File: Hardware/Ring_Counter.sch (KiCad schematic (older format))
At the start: 83 parts, among them Q10 BC848, Q11 BC848, Q12 BC848, Q13 BC848, Q14 BC848, Q15 BC848, Q16 BC848, Q17 BC848, Q18 BC848, Q19 BC848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

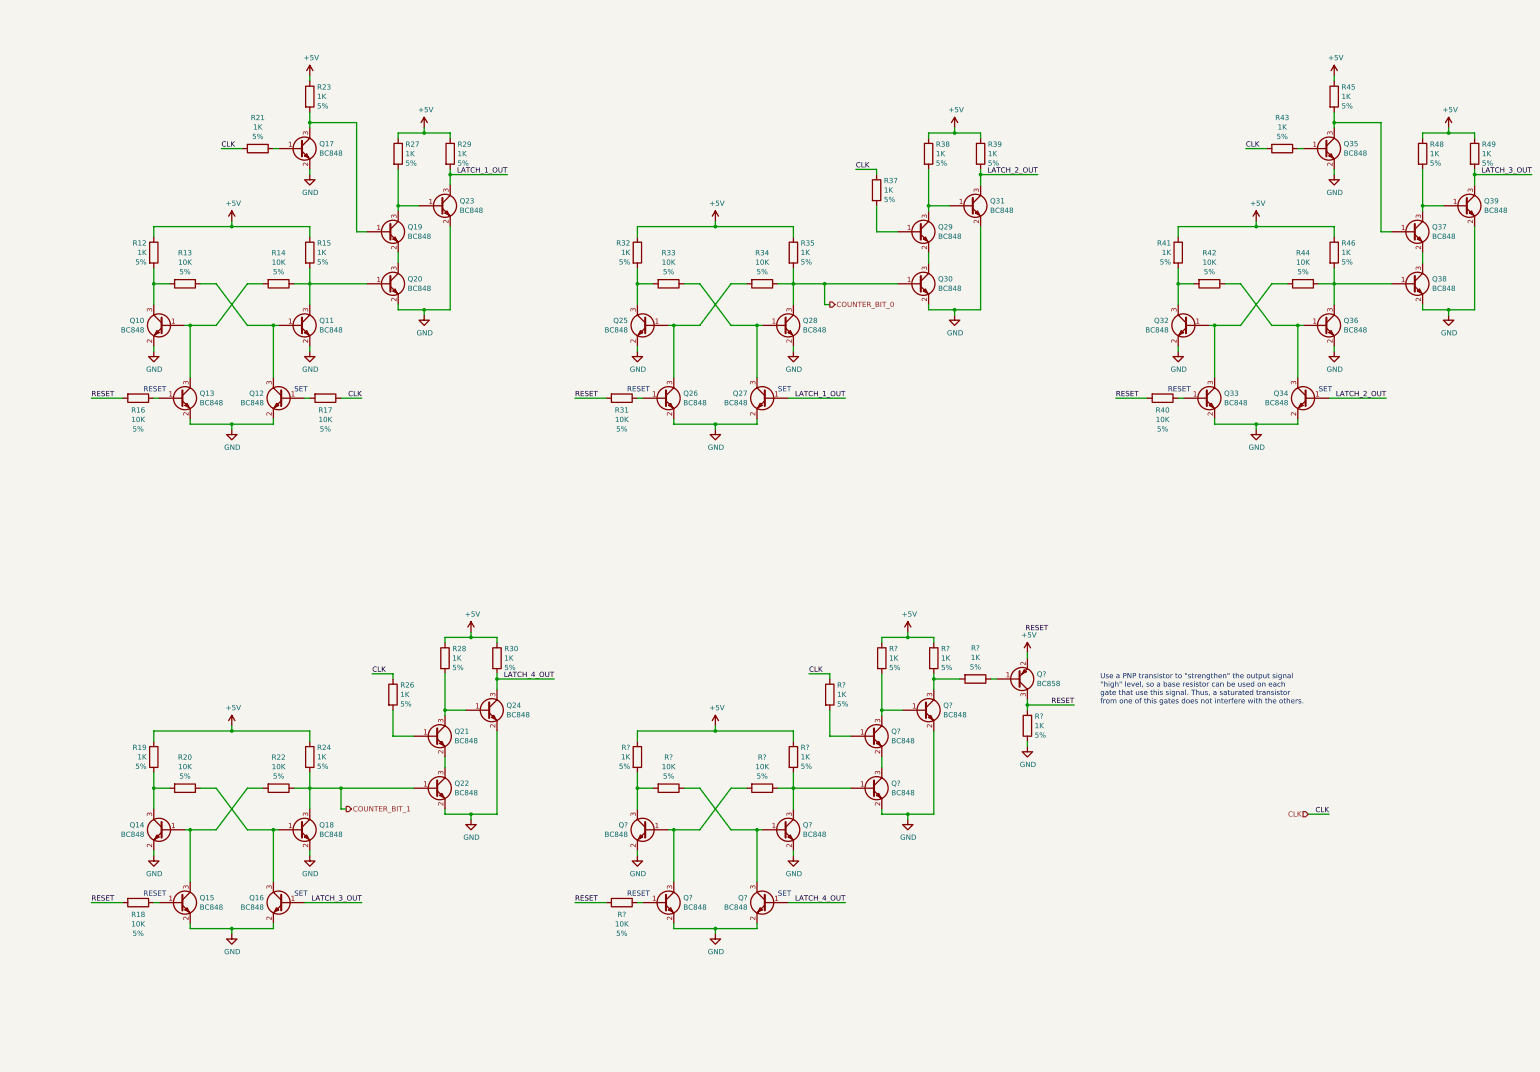
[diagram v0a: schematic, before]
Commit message: Improved ring counter RS latches output with better signal quality and less transistors count.
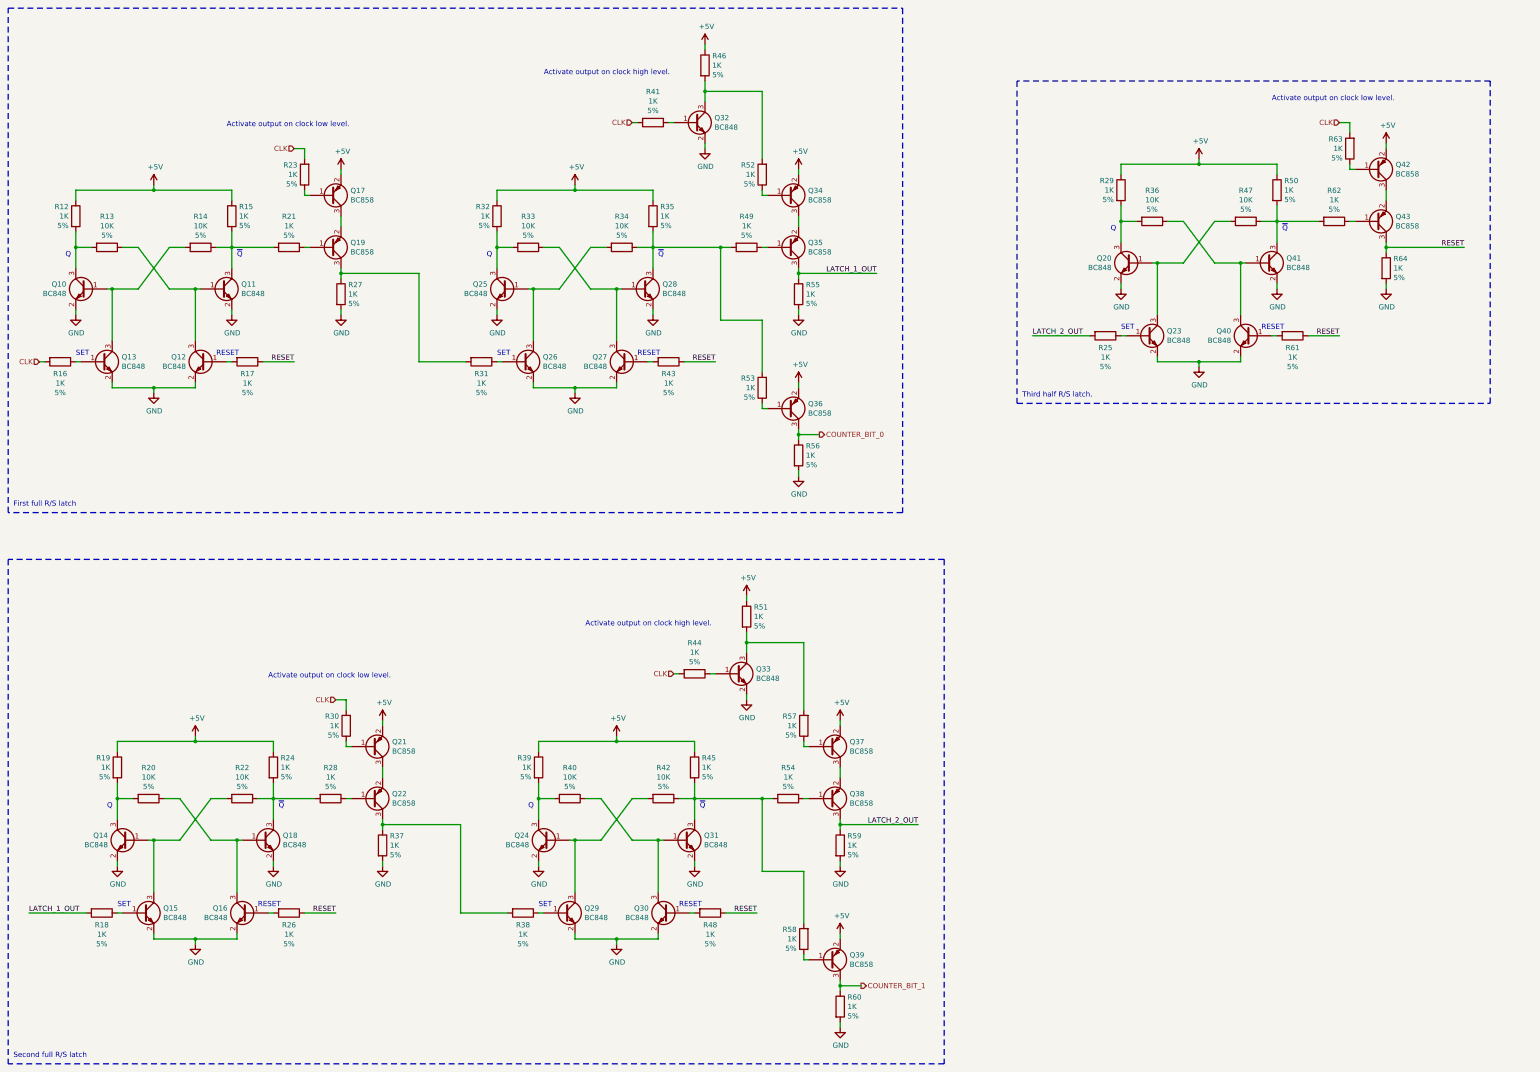
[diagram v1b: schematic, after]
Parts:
- removed Q17, Q19, Q20, Q21, Q22, Q23, Q34, Q35, Q36, Q37, Q38, Q39, Q? (x3): BC848, Package_TO_SOT_SMD:SOT-23, symbol Transistor_BJT:BC848
- removed Q?: BC858, Package_TO_SOT_SMD:SOT-23, symbol Transistor_BJT:BC858
- removed R29, R? (x5): 1K, Resistor_SMD:R_0603_1608Metric_Pad0.98x0.95mm_HandSolder, symbol Device:R
- added Q17, Q19, Q21, Q22, Q34, Q35, Q36, Q37, Q38, Q39, Q42, Q43: BC858, Package_TO_SOT_SMD:SOT-23, symbol Transistor_BJT:BC858
- added R51, R52, R53, R54, R55, R56, R57, R58, R59, R60, R61, R62, R63, R64: 1K, Resistor_SMD:R_0603_1608Metric_Pad0.98x0.95mm_HandSolder, symbol Device:R
- R16, R17, R18, R31: value 10K -> 1K
- R21, R23, R26, R28, R30, R38, R43, R48, R49: Spice_Model 1k -> 10k
- R25: renamed from R?; value 10K -> 1K
- R44: value 10K -> 1K; Spice_Model 10k -> 1k
- gave numbers to parts that had none: 8
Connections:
- net +5V: now also Q17.2 (E), Q21.2 (E), Q34.2 (E), Q36.2 (E), Q37.2 (E), Q39.2 (E), Q42.2 (E), R51.1; no longer R23.1, R27.1, R28.1, R30.1, R38.1, R41.1, R48.1, R49.1
- net CLK: now also R16.2, R23.2, R30.2, R41.2, R44.2, R63.2; no longer R17.1, R21.2, R26.1, R37.1, R43.2
- net COUNTER_BIT_0: now also Q36.3 (C), R56.1; no longer Q28.3 (C), Q30.1 (B), R34.1, R35.2
- net COUNTER_BIT_1: now also Q39.3 (C), R60.1; no longer Q18.3 (C), R22.1, R24.2
- net GND: now also Q29.2 (E), R27.2, R37.2, R55.2, R56.2, R59.2, R60.2, R64.2
- net LATCH_1_OUT: now also R18.2, Q35.3 (C), R55.1; no longer Q27.1 (B)
- net LATCH_2_OUT: now also R25.2, Q38.3 (C), R59.1; no longer Q31.3 (C), R39.2
- net RESET: now also R17.1, R26.1, R43.1, R48.1, Q43.3 (C), R61.1, R64.1; no longer R16.2, R18.2, R25.2, R31.2, R40.2
- net at Q11.3 (C), R14.1, R15.2: now also R21.2
- net at R21.1: now also Q19.1 (B)
- net at Q29.1 (B): now also R38.1; no longer R37.2
- net at Q30.3 (C): now also Q31.1 (B), R40.1; no longer Q29.2 (E)
- net at R45.2: now also Q31.3 (C), R42.1, R54.2, R58.2
- net at R48.2: now also Q30.1 (B)
- net at R46.2: now also Q32.3 (C), R52.2; no longer R44.1
- net at Q33.1 (B): now also R44.1; no longer R40.1
- net at R26.2: now also Q16.1 (B)
- net at R28.2: now also Q18.3 (C), R22.1, R24.2; no longer Q24.1 (B)
- net at Q41.3 (C), R47.1, R50.2: now also R62.2
- net LATCH_3_OUT: no longer names the net of R49.2
- net LATCH_3_OUT: now also Q28.3 (C), R34.1, R35.2, R53.2; no longer Q16.1 (B)
- removed net LATCH_4_OUT: Q24.3 (C), Q40.1 (B), R30.2
- new net: Q19.3 (C), R27.1, R31.2
- new net: Q27.1 (B), R43.2
- new net: Q40.1 (B), R61.2
- new net: Q35.1 (B), R49.1
- new net: Q34.3 (C), Q35.2 (E)
- new net: Q34.1 (B), R52.1
- new net: Q32.1 (B), R41.1
- new net: Q36.1 (B), R53.1
- new net: Q24.1 (B), Q29.3 (C), R42.2
- new net: Q24.3 (C), R39.2, R40.2
- new net: Q22.3 (C), R37.1, R38.2
- new net: Q22.1 (B), R28.1
- new net: Q21.3 (C), Q22.2 (E)
- new net: Q21.1 (B), R30.1
- new net: Q33.3 (C), R51.2, R57.2
- new net: Q39.1 (B), R58.1
- new net: Q37.1 (B), R57.1
- new net: Q37.3 (C), Q38.2 (E)
- new net: Q38.1 (B), R54.1
- new net: Q17.3 (C), Q19.2 (E)
- new net: Q17.1 (B), R23.1
- new net: Q43.1 (B), R62.1
- new net: Q42.3 (C), Q43.2 (E)
- new net: Q42.1 (B), R63.1
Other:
- note added: "Activate output on clock high level."
- note added: "Activate output on clock low level."
- note added: "First full R/S latch"
- note added: "Q"
- note added: "Second full R/S latch"
- note added: "Third half R/S latch."
- note added: "~Q~"
- note removed: "Use a PNP transistor to "strengthen" the output signal\n"high" level, so a base resistor can be used on each\ngate that use this signal. Thus, a saturated transistor\nfrom one of this gates does not interfere with the others."
- moved on the sheet: Q10, Q11, Q12, Q13, Q20, Q23, Q25, Q26, Q27, Q28, Q40, Q41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

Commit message: Added second led logic and power transistor, also added BC858 SPICE model.
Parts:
- Q17, Q19, Q21, Q22, Q34, Q35, Q36, Q37, Q38, Q39, Q42, Q43: Spice_Lib_File (none) -> Spice_Simulation/BC858.lib; Spice_Model (none) -> BC858; Spice_Netlist_Enabled (none) -> Y; Spice_Node_Sequence (none) -> 3 1 2; Spice_Primitive (none) -> Q
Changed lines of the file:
@@
 F 2 "Package_TO_SOT_SMD:SOT-23" H 3900 2975 50  0001 L CIN
 F 3 "https://www.onsemi.com/pub/Collateral/BC860-D.pdf" H 3700 3050 50  0001 L CNN
+F 4 "Spice_Simulation/BC858.lib" H 3700 3050 50  0001 C CNN "Spice_Lib_File"
+F 5 "BC858" H 3700 3050 50  0001 C CNN "Spice_Model"
+F 6 "Y" H 3700 3050 50  0001 C CNN "Spice_Netlist_Enabled"
+F 7 "Q" H 3700 3050 50  0001 C CNN "Spice_Primitive"
+F 8 "3 1 2" H 3700 3050 50  0001 C CNN "Spice_Node_Sequence"
 	1    3700 3050
 	1    0    0    1
@@
 F 2 "Package_TO_SOT_SMD:SOT-23" H 3900 2475 50  0001 L CIN
 F 3 "https://www.onsemi.com/pub/Collateral/BC860-D.pdf" H 3700 2550 50  0001 L CNN
+F 4 "Q" H 3700 2550 50  0001 C CNN "Spice_Primitive"
+F 5 "BC858" H 3700 2550 50  0001 C CNN "Spice_Model"
+F 6 "Y" H 3700 2550 50  0001 C CNN "Spice_Netlist_Enabled"
+F 7 "Spice_Simulation/BC858.lib" H 3700 2550 50  0001 C CNN "Spice_Lib_File"
+F 8 "3 1 2" H 3700 2550 50  0001 C CNN "Spice_Node_Sequence"
 	1    3700 2550
 	1    0    0    1
@@
 F 2 "Package_TO_SOT_SMD:SOT-23" H 8300 4525 50  0001 L CIN
 F 3 "https://www.onsemi.com/pub/Collateral/BC860-D.pdf" H 8100 4600 50  0001 L CNN
+F 4 "Spice_Simulation/BC858.lib" H 8100 4600 50  0001 C CNN "Spice_Lib_File"
+F 5 "BC858" H 8100 4600 50  0001 C CNN "Spice_Model"
+F 6 "Y" H 8100 4600 50  0001 C CNN "Spice_Netlist_Enabled"
+F 7 "Q" H 8100 4600 50  0001 C CNN "Spice_Primitive"
+F 8 "3 1 2" H 8100 4600 50  0001 C CNN "Spice_Node_Sequence"
 	1    8100 4600
 	1    0    0    1
@@
 F 2 "Package_TO_SOT_SMD:SOT-23" H 8300 2475 50  0001 L CIN
 F 3 "https://www.onsemi.com/pub/Collateral/BC860-D.pdf" H 8100 2550 50  0001 L CNN
+F 4 "Spice_Simulation/BC858.lib" H 8100 2550 50  0001 C CNN "Spice_Lib_File"
+F 5 "BC858" H 8100 2550 50  0001 C CNN "Spice_Model"
+F 6 "Y" H 8100 2550 50  0001 C CNN "Spice_Netlist_Enabled"
+F 7 "Q" H 8100 2550 50  0001 C CNN "Spice_Primitive"
+F 8 "3 1 2" H 8100 2550 50  0001 C CNN "Spice_Node_Sequence"
 	1    8100 2550
 	1    0    0    1
@@
 F 2 "Package_TO_SOT_SMD:SOT-23" H 8300 2975 50  0001 L CIN
 F 3 "https://www.onsemi.com/pub/Collateral/BC860-D.pdf" H 8100 3050 50  0001 L CNN
+F 4 "Spice_Simulation/BC858.lib" H 8100 3050 50  0001 C CNN "Spice_Lib_File"
+F 5 "BC858" H 8100 3050 50  0001 C CNN "Spice_Model"
+F 6 "Y" H 8100 3050 50  0001 C CNN "Spice_Netlist_Enabled"
+F 7 "Q" H 8100 3050 50  0001 C CNN "Spice_Primitive"
+F 8 "3 1 2" H 8100 3050 50  0001 C CNN "Spice_Node_Sequence"
 	1    8100 3050
 	1    0    0    1
@@
 F 2 "Package_TO_SOT_SMD:SOT-23" H 4300 8275 50  0001 L CIN
 F 3 "https://www.onsemi.com/pub/Collateral/BC860-D.pdf" H 4100 8350 50  0001 L CNN
+F 4 "Spice_Simulation/BC858.lib" H 4100 8350 50  0001 C CNN "Spice_Lib_File"
+F 5 "BC858" H 4100 8350 50  0001 C CNN "Spice_Model"
+F 6 "Y" H 4100 8350 50  0001 C CNN "Spice_Netlist_Enabled"
+F 7 "Q" H 4100 8350 50  0001 C CNN "Spice_Primitive"
+F 8 "3 1 2" H 4100 8350 50  0001 C CNN "Spice_Node_Sequence"
 	1    4100 8350
 	1    0    0    1
@@
 F 2 "Package_TO_SOT_SMD:SOT-23" H 4300 7775 50  0001 L CIN
 F 3 "https://www.onsemi.com/pub/Collateral/BC860-D.pdf" H 4100 7850 50  0001 L CNN
+F 4 "Spice_Simulation/BC858.lib" H 4100 7850 50  0001 C CNN "Spice_Lib_File"
+F 5 "BC858" H 4100 7850 50  0001 C CNN "Spice_Model"
+F 6 "Y" H 4100 7850 50  0001 C CNN "Spice_Netlist_Enabled"
+F 7 "Q" H 4100 7850 50  0001 C CNN "Spice_Primitive"
+F 8 "3 1 2" H 4100 7850 50  0001 C CNN "Spice_Node_Sequence"
 	1    4100 7850
 	1    0    0    1
@@
 F 2 "Package_TO_SOT_SMD:SOT-23" H 8700 9825 50  0001 L CIN
 F 3 "https://www.onsemi.com/pub/Collateral/BC860-D.pdf" H 8500 9900 50  0001 L CNN
+F 4 "Spice_Simulation/BC858.lib" H 8500 9900 50  0001 C CNN "Spice_Lib_File"
+F 5 "BC858" H 8500 9900 50  0001 C CNN "Spice_Model"
+F 6 "Y" H 8500 9900 50  0001 C CNN "Spice_Netlist_Enabled"
+F 7 "Q" H 8500 9900 50  0001 C CNN "Spice_Primitive"
+F 8 "3 1 2" H 8500 9900 50  0001 C CNN "Spice_Node_Sequence"
 	1    8500 9900
 	1    0    0    1
@@
 F 2 "Package_TO_SOT_SMD:SOT-23" H 8700 7775 50  0001 L CIN
 F 3 "https://www.onsemi.com/pub/Collateral/BC860-D.pdf" H 8500 7850 50  0001 L CNN
+F 4 "Spice_Simulation/BC858.lib" H 8500 7850 50  0001 C CNN "Spice_Lib_File"
+F 5 "BC858" H 8500 7850 50  0001 C CNN "Spice_Model"
+F 6 "Y" H 8500 7850 50  0001 C CNN "Spice_Netlist_Enabled"
+F 7 "Q" H 8500 7850 50  0001 C CNN "Spice_Primitive"
+F 8 "3 1 2" H 8500 7850 50  0001 C CNN "Spice_Node_Sequence"
 	1    8500 7850
 	1    0    0    1
@@
 F 2 "Package_TO_SOT_SMD:SOT-23" H 8700 8275 50  0001 L CIN
 F 3 "https://www.onsemi.com/pub/Collateral/BC860-D.pdf" H 8500 8350 50  0001 L CNN
+F 4 "Spice_Simulation/BC858.lib" H 8500 8350 50  0001 C CNN "Spice_Lib_File"
+F 5 "BC858" H 8500 8350 50  0001 C CNN "Spice_Model"
+F 6 "Y" H 8500 8350 50  0001 C CNN "Spice_Netlist_Enabled"
+F 7 "Q" H 8500 8350 50  0001 C CNN "Spice_Primitive"
+F 8 "3 1 2" H 8500 8350 50  0001 C CNN "Spice_Node_Sequence"
 	1    8500 8350
 	1    0    0    1
@@
 F 2 "Package_TO_SOT_SMD:SOT-23" H 13950 2725 50  0001 L CIN
 F 3 "https://www.onsemi.com/pub/Collateral/BC860-D.pdf" H 13750 2800 50  0001 L CNN
+F 4 "Spice_Simulation/BC858.lib" H 13750 2800 50  0001 C CNN "Spice_Lib_File"
+F 5 "BC858" H 13750 2800 50  0001 C CNN "Spice_Model"
+F 6 "Y" H 13750 2800 50  0001 C CNN "Spice_Netlist_Enabled"
+F 7 "Q" H 13750 2800 50  0001 C CNN "Spice_Primitive"
+F 8 "3 1 2" H 13750 2800 50  0001 C CNN "Spice_Node_Sequence"
 	1    13750 2800
 	1    0    0    1
@@
 F 2 "Package_TO_SOT_SMD:SOT-23" H 13950 2225 50  0001 L CIN
 F 3 "https://www.onsemi.com/pub/Collateral/BC860-D.pdf" H 13750 2300 50  0001 L CNN
+F 4 "Spice_Simulation/BC858.lib" H 13750 2300 50  0001 C CNN "Spice_Lib_File"
+F 5 "BC858" H 13750 2300 50  0001 C CNN "Spice_Model"
+F 6 "Y" H 13750 2300 50  0001 C CNN "Spice_Netlist_Enabled"
+F 7 "Q" H 13750 2300 50  0001 C CNN "Spice_Primitive"
+F 8 "3 1 2" H 13750 2300 50  0001 C CNN "Spice_Node_Sequence"
 	1    13750 2300
 	1    0    0    1

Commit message: Added RS latches power-on reset.
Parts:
- added C1: 4.7u, Capacitor_SMD:C_0805_2012Metric_Pad1.18x1.45mm_HandSolder, symbol Device:C
- added Q46: BC858, Package_TO_SOT_SMD:SOT-23, symbol Transistor_BJT:BC858
- added R70: 220K, Resistor_SMD:R_0603_1608Metric_Pad0.98x0.95mm_HandSolder, symbol Device:R
- added R71: 1K, Resistor_SMD:R_0603_1608Metric_Pad0.98x0.95mm_HandSolder, symbol Device:R
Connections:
- net +5V: now also Q46.2 (E), R70.2
- net GND: now also C1.2
- net RESET: now also Q46.3 (C)
- new net: C1.1, R70.1, R71.2
- new net: Q46.1 (B), R71.1
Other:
- note added: "First full RS latch."
- note added: "Power-on reset\nGenerate a 100ms high level pulse to reset latches."
- note added: "Second full RS latch."
- note added: "Third half RS latch."
- note removed: "First full R/S latch"
- note removed: "Second full R/S latch"
- note removed: "Third half R/S latch."
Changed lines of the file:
@@
 	600  5600 600  750
 Text Notes 650  5550 0    50   ~ 0
-First full R/S latch
+First full RS latch.
 Wire Notes Line
 	9600 6050 9600 10900
@@
 	600  6050 600  10900
 Text Notes 650  10850 0    50   ~ 0
-Second full R/S latch
+Second full RS latch.
 Text Label 9350 8600 2    50   ~ 0
 LATCH_2_OUT
@@
 	10300 4550 14850 4550
 Text Notes 10350 4500 0    50   ~ 0
-Third half R/S latch.
+Third half RS latch.
+$Comp
+L Device:R R?
+U 1 1 6211682E
+P 12300 7400
+AR Path="/6211682E" Ref="R?"  Part="1"
+AR Path="/61D90E9A/6211682E" Ref="R70"  Part="1"
+F 0 "R70" V 12003 7400 50  0000 C CNN
+F 1 "220K" V 12094 7400 50  0000 C CNN
+F 2 "Resistor_SMD:R_0603_1608Metric_Pad0.98x0.95mm_HandSolder" V 12230 7400 50  0001 C CNN
+F 3 "~" H 12300 7400 50  0001 C CNN
+F 4 "5%" V 12185 7400 50  0000 C CNN "Value2"
+F 5 "R" H 12300 7400 50  0001 C CNN "Spice_Primitive"
+F 6 "1k" H 12300 7400 50  0001 C CNN "Spice_Model"
+F 7 "Y" H 12300 7400 50  0001 C CNN "Spice_Netlist_Enabled"
+	1    12300 7400
+	0    1    1    0
+$EndComp
+$Comp
+L Device:C C1
+U 1 1 62117E9F
+P 12700 7650
+F 0 "C1" H 12815 7787 50  0000 L CNN
+F 1 "4.7u" H 12815 7696 50  0000 L CNN
+F 2 "Capacitor_SMD:C_0805_2012Metric_Pad1.18x1.45mm_HandSolder" H 12738 7500 50  0001 C CNN
+F 3 "~" H 12700 7650 50  0001 C CNN
+F 4 "16V" H 12815 7605 50  0000 L CNN "Value2"
+F 5 "X5R" H 12815 7514 50  0000 L CNN "Value3"
+F 6 "CL21A475KOFNNNE" H 12700 7650 50  0001 C CNN "PartNumber"
+F 7 "Samsung" H 12700 7650 50  0001 C CNN "Manufacturer"
+	1    12700 7650
+	1    0    0    -1
+$EndComp
+$Comp
+L Device:R R?
+U 1 1 6211A796
+P 13100 7400
+AR Path="/6211A796" Ref="R?"  Part="1"
+AR Path="/61D90E9A/6211A796" Ref="R71"  Part="1"
+F 0 "R71" V 12803 7400 50  0000 C CNN
+F 1 "1K" V 12894 7400 50  0000 C CNN
+F 2 "Resistor_SMD:R_0603_1608Metric_Pad0.98x0.95mm_HandSolder" V 13030 7400 50  0001 C CNN
+F 3 "~" H 13100 7400 50  0001 C CNN
+F 4 "5%" V 12985 7400 50  0000 C CNN "Value2"
+F 5 "R" H 13100 7400 50  0001 C CNN "Spice_Primitive"
+F 6 "1k" H 13100 7400 50  0001 C CNN "Spice_Model"
+F 7 "Y" H 13100 7400 50  0001 C CNN "Spice_Netlist_Enabled"
+	1    13100 7400
+	0    1    1    0
+$EndComp
+$Comp
+L Transistor_BJT:BC858 Q46
+U 1 1 6211DBE2
+P 13500 7400
+F 0 "Q46" H 13691 7354 50  0000 L CNN
+F 1 "BC858" H 13691 7445 50  0000 L CNN
+F 2 "Package_TO_SOT_SMD:SOT-23" H 13700 7325 50  0001 L CIN
+F 3 "https://www.onsemi.com/pub/Collateral/BC860-D.pdf" H 13500 7400 50  0001 L CNN
+F 4 "Spice_Simulation/BC858.lib" H 13500 7400 50  0001 C CNN "Spice_Lib_File"
+F 5 "BC858" H 13500 7400 50  0001 C CNN "Spice_Model"
+F 6 "Y" H 13500 7400 50  0001 C CNN "Spice_Netlist_Enabled"
+F 7 "Q" H 13500 7400 50  0001 C CNN "Spice_Primitive"
+F 8 "3 1 2" H 13500 7400 50  0001 C CNN "Spice_Node_Sequence"
+	1    13500 7400
+	1    0    0    1
+$EndComp
+$Comp
+L power:+5V #PWR?
+U 1 1 6212D299
+P 13600 7100
+AR Path="/6212D299" Ref="#PWR?"  Part="1"
+AR Path="/61D90E9A/6212D299" Ref="#PWR061"  Part="1"
+F 0 "#PWR061" H 13600 6950 50  0001 C CNN
+F 1 "+5V" H 13615 7273 50  0000 C CNN
+F 2 "" H 13600 7100 50  0001 C CNN
+F 3 "" H 13600 7100 50  0001 C CNN
+F 4 "V" H 13600 7100 50  0001 C CNN "Spice_Primitive"
+F 5 "dc 5" H 13600 7100 50  0001 C CNN "Spice_Model"
+F 6 "Y" H 13600 7100 50  0001 C CNN "Spice_Netlist_Enabled"
+	1    13600 7100
+	1    0    0    -1
+$EndComp
+Text Label 13950 7800 2    50   ~ 0
+RESET
+Wire Wire Line
+	13600 7600 13600 7800
+Wire Wire Line
+	13600 7800 13950 7800
+Wire Wire Line
+	13250 7400 13300 7400
+Wire Wire Line
+	12450 7400 12700 7400
+Wire Wire Line
+	12700 7500 12700 7400
+Connection ~ 12700 7400
+Wire Wire Line
+	12700 7400 12950 7400
+Wire Wire Line
+	13600 7100 13600 7200
+$Comp
+L power:+5V #PWR?
+U 1 1 62180E8E
+P 11950 7350
+AR Path="/62180E8E" Ref="#PWR?"  Part="1"
+AR Path="/61D90E9A/62180E8E" Ref="#PWR059"  Part="1"
+F 0 "#PWR059" H 11950 7200 50  0001 C CNN
+F 1 "+5V" H 11965 7523 50  0000 C CNN
+F 2 "" H 11950 7350 50  0001 C CNN
+F 3 "" H 11950 7350 50  0001 C CNN
+F 4 "V" H 11950 7350 50  0001 C CNN "Spice_Primitive"
+F 5 "dc 5" H 11950 7350 50  0001 C CNN "Spice_Model"
+F 6 "Y" H 11950 7350 50  0001 C CNN "Spice_Netlist_Enabled"
+	1    11950 7350
+	1    0    0    -1
+$EndComp
+Wire Wire Line
+	11950 7400 12150 7400
+$Comp
+L power:GND #PWR060
+U 1 1 621A1546
+P 12700 7850
+F 0 "#PWR060" H 12700 7600 50  0001 C CNN
+F 1 "GND" H 12705 7677 50  0000 C CNN
+F 2 "" H 12700 7850 50  0001 C CNN
+F 3 "" H 12700 7850 50  0001 C CNN
+	1    12700 7850
+	1    0    0    -1
+$EndComp
+Wire Wire Line
+	12700 7800 12700 7850
+Wire Notes Line
+	11500 6700 14200 6700
+Wire Notes Line
+	14200 6700 14200 8600
+Wire Notes Line
+	14200 8600 11500 8600
+Wire Notes Line
+	11500 8600 11500 6700
+Text Notes 11600 8550 0    50   ~ 0
+Power-on reset\nGenerate a 100ms high level pulse to reset latches.
+Wire Wire Line
+	11950 7400 11950 7350
 $EndSCHEMATC
